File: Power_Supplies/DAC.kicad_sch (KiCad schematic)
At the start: 49 parts, among them J1 Line Out (Left), J2 Headphone Out, J21 Line Out (Right), U10 OPA2134, U11 TPA6110A2DGN, U34 NE5532AD, U35 NE5532AD, U9 PCM1780

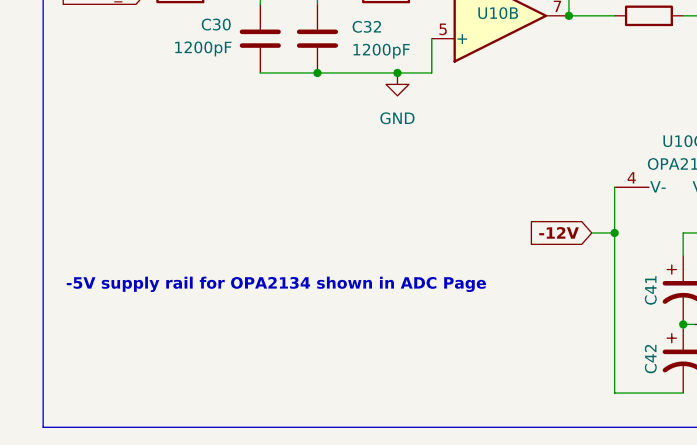
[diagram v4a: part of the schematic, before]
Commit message: Add files via upload
fixed voltage issues
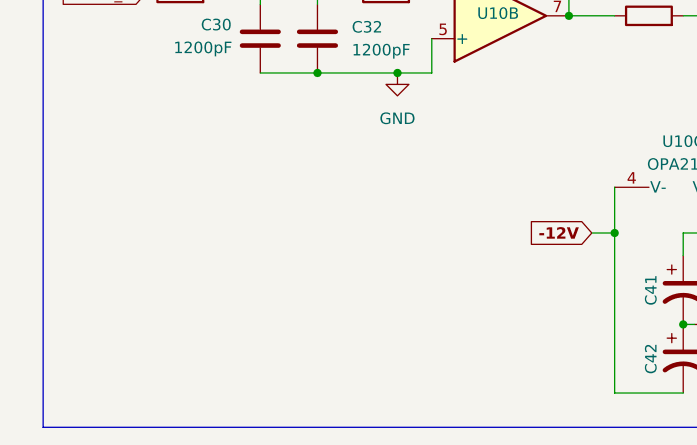
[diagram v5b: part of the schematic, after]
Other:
- note removed: "-5V supply rail for OPA2134 shown in ADC Page"
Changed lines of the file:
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@@
 		)
 	)
-	(text "-5V supply rail for OPA2134 shown in ADC Page\n"
-		(exclude_from_sim no)
-		(at 41.148 179.832 0)
-		(effects
-			(font
-				(size 1.27 1.27)
-				(bold yes)
-			)
-		)
-	)
 	(text "Headphone Amplifier \nUsing EVM Schematic as Ref.\n"
 		(exclude_from_sim no)
@@
 		(exclude_from_sim no)
 		(in_bom yes)
-		(on_board no)
+		(on_board yes)
 		(dnp no)
 		(fields_autoplaced yes)
@@
 		(exclude_from_sim no)
 		(in_bom yes)
-		(on_board no)
+		(on_board yes)
 		(dnp no)
 		(fields_autoplaced yes)
@@
 		(exclude_from_sim no)
 		(in_bom yes)
-		(on_board no)
+		(on_board yes)
 		(dnp no)
 		(fields_autoplaced yes)
@@
 		(exclude_from_sim no)
 		(in_bom yes)
-		(on_board no)
+		(on_board yes)
 		(dnp no)
 		(property "Reference" "C42"
@@
 		(exclude_from_sim no)
 		(in_bom yes)
-		(on_board no)
+		(on_board yes)
 		(dnp no)
 		(property "Reference" "C43"
@@
 		(exclude_from_sim no)
 		(in_bom yes)
-		(on_board no)
+		(on_board yes)
 		(dnp no)
 		(fields_autoplaced yes)
@@
 		(exclude_from_sim no)
 		(in_bom yes)
-		(on_board no)
+		(on_board yes)
 		(dnp no)
 		(property "Reference" "U34"
@@
 		(exclude_from_sim no)
 		(in_bom yes)
-		(on_board no)
+		(on_board yes)
 		(dnp no)
 		(fields_autoplaced yes)
@@
 		(exclude_from_sim no)
 		(in_bom yes)
-		(on_board no)
+		(on_board yes)
 		(dnp no)
 		(fields_autoplaced yes)
@@
 		(exclude_from_sim no)
 		(in_bom yes)
-		(on_board no)
+		(on_board yes)
 		(dnp no)
 		(property "Reference" "C41"
@@
 		(exclude_from_sim no)
 		(in_bom yes)
-		(on_board no)
+		(on_board yes)
 		(dnp no)
 		(property "Reference" "R24"
@@
 		(exclude_from_sim no)
 		(in_bom yes)
-		(on_board no)
+		(on_board yes)
 		(dnp no)
 		(property "Reference" "C33"
@@
 		(exclude_from_sim no)
 		(in_bom yes)
-		(on_board no)
+		(on_board yes)
 		(dnp no)
 		(fields_autoplaced yes)
@@
 		(exclude_from_sim no)
 		(in_bom yes)
-		(on_board no)
+		(on_board yes)
 		(dnp no)
 		(fields_autoplaced yes)
@@
 		(exclude_from_sim no)
 		(in_bom yes)
-		(on_board no)
+		(on_board yes)
 		(dnp no)
 		(property "Reference" "C29"
@@
 		(exclude_from_sim no)
 		(in_bom yes)
-		(on_board no)
+		(on_board yes)
 		(dnp no)
 		(property "Reference" "#PWR036"
@@
 		(exclude_from_sim no)
 		(in_bom yes)
-		(on_board no)
+		(on_board yes)
 		(dnp no)
 		(fields_autoplaced yes)
@@
 		(exclude_from_sim no)
 		(in_bom yes)
-		(on_board no)
+		(on_board yes)
 		(dnp no)
 		(fields_autoplaced yes)
@@
 		(exclude_from_sim no)
 		(in_bom yes)
-		(on_board no)
+		(on_board yes)
 		(dnp no)
 		(fields_autoplaced yes)
@@
 		(exclude_from_sim no)
 		(in_bom yes)
-		(on_board no)
+		(on_board yes)
 		(dnp no)
 		(fields_autoplaced yes)
@@
 		(exclude_from_sim no)
 		(in_bom yes)
-		(on_board no)
+		(on_board yes)
 		(dnp no)
 		(fields_autoplaced yes)
@@
 		(exclude_from_sim no)
 		(in_bom yes)
-		(on_board no)
+		(on_board yes)
 		(dnp no)
 		(property "Reference" "U10"
@@
 		(exclude_from_sim no)
 		(in_bom yes)
-		(on_board no)
+		(on_board yes)
 		(dnp no)
 		(fields_autoplaced yes)
@@
 		(exclude_from_sim no)
 		(in_bom yes)
-		(on_board no)
+		(on_board yes)
 		(dnp no)
 		(property "Reference" "C35"
@@
 		(exclude_from_sim no)
 		(in_bom yes)
-		(on_board no)
+		(on_board yes)
 		(dnp no)
 		(property "Reference" "U11"
@@
 		(exclude_from_sim no)
 		(in_bom yes)
-		(on_board no)
+		(on_board yes)
 		(dnp no)
 		(property "Reference" "R26"
@@
 		(exclude_from_sim no)
 		(in_bom yes)
-		(on_board no)
+		(on_board yes)
 		(dnp no)
 		(fields_autoplaced yes)
@@
 		(exclude_from_sim no)
 		(in_bom yes)
-		(on_board no)
+		(on_board yes)
 		(dnp no)
 		(fields_autoplaced yes)
@@
 		(exclude_from_sim no)
 		(in_bom yes)
-		(on_board no)
+		(on_board yes)
 		(dnp no)
 		(property "Reference" "C34"
@@
 		(exclude_from_sim no)
 		(in_bom yes)
-		(on_board no)
+		(on_board yes)
 		(dnp no)
 		(fields_autoplaced yes)
@@
 		(exclude_from_sim no)
 		(in_bom yes)
-		(on_board no)
+		(on_board yes)
 		(dnp no)
 		(property "Reference" "R30"
@@
 		(exclude_from_sim no)
 		(in_bom yes)
-		(on_board no)
+		(on_board yes)
 		(dnp no)
 		(fields_autoplaced yes)
@@
 		(exclude_from_sim no)
 		(in_bom yes)
-		(on_board no)
+		(on_board yes)
 		(dnp no)
 		(property "Reference" "R32"
@@
 		(exclude_from_sim no)
 		(in_bom yes)
-		(on_board no)
+		(on_board yes)
 		(dnp no)
 		(property "Reference" "U10"
@@
 		(exclude_from_sim no)
 		(in_bom yes)
-		(on_board no)
+		(on_board yes)
 		(dnp no)
 		(fields_autoplaced yes)
@@
 		(exclude_from_sim no)
 		(in_bom yes)
-		(on_board no)
+		(on_board yes)
 		(dnp no)
 		(fields_autoplaced yes)
@@
 		(exclude_from_sim no)
 		(in_bom yes)
-		(on_board no)
+		(on_board yes)
 		(dnp no)
 		(fields_autoplaced yes)
@@
 		(exclude_from_sim no)
 		(in_bom yes)
-		(on_board no)
+		(on_board yes)
 		(dnp no)
 		(property "Reference" "#PWR044"
@@
 		(exclude_from_sim no)
 		(in_bom yes)
-		(on_board no)
+		(on_board yes)
 		(dnp no)
 		(property "Reference" "U35"
@@
 		(exclude_from_sim no)
 		(in_bom yes)
-		(on_board no)
+		(on_board yes)
 		(dnp no)
 		(property "Reference" "R20"
@@
 		(exclude_from_sim no)
 		(in_bom yes)
-		(on_board no)
+		(on_board yes)
 		(dnp no)
 		(property "Reference" "C30"
@@
 		(exclude_from_sim no)
 		(in_bom yes)
-		(on_board no)
+		(on_board yes)
 		(dnp no)
 		(property "Reference" "R21"
@@
 		(exclude_from_sim no)
 		(in_bom yes)
-		(on_board no)
+		(on_board yes)
 		(dnp no)
 		(fields_autoplaced yes)
@@
 		(exclude_from_sim no)
 		(in_bom yes)
-		(on_board no)
+		(on_board yes)
 		(dnp no)
 		(property "Reference" "R22"
@@
 		(exclude_from_sim no)
 		(in_bom yes)
-		(on_board no)
+		(on_board yes)
 		(dnp no)
 		(fields_autoplaced yes)
@@
 		(exclude_from_sim no)
 		(in_bom yes)
-		(on_board no)
+		(on_board yes)
 		(dnp no)
 		(fields_autoplaced yes)
@@
 		(exclude_from_sim no)
 		(in_bom yes)
-		(on_board no)
+		(on_board yes)
 		(dnp no)
 		(fields_autoplaced yes)
@@
 		(exclude_from_sim no)
 		(in_bom yes)
-		(on_board no)
+		(on_board yes)
 		(dnp no)
 		(fields_autoplaced yes)
@@
 		(exclude_from_sim no)
 		(in_bom yes)
-		(on_board no)
+		(on_board yes)
 		(dnp no)
 		(fields_autoplaced yes)
@@
 		(exclude_from_sim no)
 		(in_bom yes)
-		(on_board no)
+		(on_board yes)
 		(dnp no)
 		(property "Reference" "R19"
@@
 		(exclude_from_sim no)
 		(in_bom yes)
-		(on_board no)
+		(on_board yes)
 		(dnp no)
 		(fields_autoplaced yes)
@@
 		(exclude_from_sim no)
 		(in_bom yes)
-		(on_board no)
+		(on_board yes)
 		(dnp no)
 		(property "Reference" "C40"
@@
 		(exclude_from_sim no)
 		(in_bom yes)
-		(on_board no)
+		(on_board yes)
 		(dnp no)
 		(property "Reference" "C47"
@@
 		(exclude_from_sim no)
 		(in_bom yes)
-		(on_board no)
+		(on_board yes)
 		(dnp no)
 		(fields_autoplaced yes)
@@
 		(exclude_from_sim no)
 		(in_bom yes)
-		(on_board no)
+		(on_board yes)
 		(dnp no)
 		(fields_autoplaced yes)
@@
 		(exclude_from_sim no)
 		(in_bom yes)
-		(on_board no)
+		(on_board yes)
 		(dnp no)
 		(property "Reference" "C39"
@@
 		(exclude_from_sim no)
 		(in_bom yes)
-		(on_board no)
+		(on_board yes)
 		(dnp no)
 		(property "Reference" "U10"
@@
 		(exclude_from_sim no)
 		(in_bom yes)
-		(on_board no)
+		(on_board yes)
 		(dnp no)
 		(fields_autoplaced yes)
@@
 		(exclude_from_sim no)
 		(in_bom yes)
-		(on_board no)
+		(on_board yes)
 		(dnp no)
 		(property "Reference" "R23"
@@
 		(exclude_from_sim no)
 		(in_bom yes)
-		(on_board no)
+		(on_board yes)
 		(dnp no)
 		(property "Reference" "C45"
@@
 		(exclude_from_sim no)
 		(in_bom yes)
-		(on_board no)
+		(on_board yes)
 		(dnp no)
 		(property "Reference" "R25"
@@
 		(exclude_from_sim no)
 		(in_bom yes)
-		(on_board no)
+		(on_board yes)
 		(dnp no)
 		(fields_autoplaced yes)
@@
 		(exclude_from_sim no)
 		(in_bom yes)
-		(on_board no)
+		(on_board yes)
 		(dnp no)
 		(fields_autoplaced yes)
@@
 		(exclude_from_sim no)
 		(in_bom yes)
-		(on_board no)
+		(on_board yes)
 		(dnp no)
 		(fields_autoplaced yes)
@@
 		(exclude_from_sim no)
 		(in_bom yes)
-		(on_board no)
+		(on_board yes)
 		(dnp no)
 		(property "Reference" "C36"
@@
 		(exclude_from_sim no)
 		(in_bom yes)
-		(on_board no)
+		(on_board yes)
 		(dnp no)
 		(fields_autoplaced yes)

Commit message: connected ADC/DACs, USB
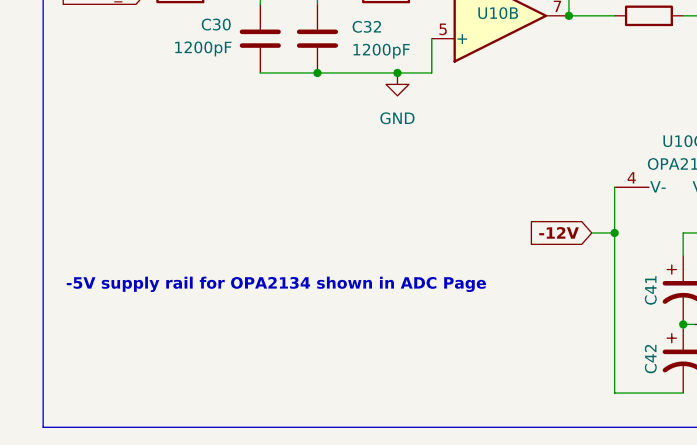
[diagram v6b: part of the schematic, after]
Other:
- note added: "-5V supply rail for OPA2134 shown in ADC Page"
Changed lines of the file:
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@@
 		)
 	)
+	(text "-5V supply rail for OPA2134 shown in ADC Page\n"
+		(exclude_from_sim no)
+		(at 41.148 179.832 0)
+		(effects
+			(font
+				(size 1.27 1.27)
+				(bold yes)
+			)
+		)
+	)
 	(text "Headphone Amplifier \nUsing EVM Schematic as Ref.\n"
 		(exclude_from_sim no)
@@
 		(exclude_from_sim no)
 		(in_bom yes)
-		(on_board yes)
+		(on_board no)
 		(dnp no)
 		(fields_autoplaced yes)
@@
 		(exclude_from_sim no)
 		(in_bom yes)
-		(on_board yes)
+		(on_board no)
 		(dnp no)
 		(fields_autoplaced yes)
@@
 		(exclude_from_sim no)
 		(in_bom yes)
-		(on_board yes)
+		(on_board no)
 		(dnp no)
 		(fields_autoplaced yes)
@@
 		(exclude_from_sim no)
 		(in_bom yes)
-		(on_board yes)
+		(on_board no)
 		(dnp no)
 		(property "Reference" "C42"
@@
 		(exclude_from_sim no)
 		(in_bom yes)
-		(on_board yes)
+		(on_board no)
 		(dnp no)
 		(property "Reference" "C43"
@@
 		(exclude_from_sim no)
 		(in_bom yes)
-		(on_board yes)
+		(on_board no)
 		(dnp no)
 		(fields_autoplaced yes)
@@
 		(exclude_from_sim no)
 		(in_bom yes)
-		(on_board yes)
+		(on_board no)
 		(dnp no)
 		(property "Reference" "U34"
@@
 		(exclude_from_sim no)
 		(in_bom yes)
-		(on_board yes)
+		(on_board no)
 		(dnp no)
 		(fields_autoplaced yes)
@@
 		(exclude_from_sim no)
 		(in_bom yes)
-		(on_board yes)
+		(on_board no)
 		(dnp no)
 		(fields_autoplaced yes)
@@
 		(exclude_from_sim no)
 		(in_bom yes)
-		(on_board yes)
+		(on_board no)
 		(dnp no)
 		(property "Reference" "C41"
@@
 		(exclude_from_sim no)
 		(in_bom yes)
-		(on_board yes)
+		(on_board no)
 		(dnp no)
 		(property "Reference" "R24"
@@
 		(exclude_from_sim no)
 		(in_bom yes)
-		(on_board yes)
+		(on_board no)
 		(dnp no)
 		(property "Reference" "C33"
@@
 		(exclude_from_sim no)
 		(in_bom yes)
-		(on_board yes)
+		(on_board no)
 		(dnp no)
 		(fields_autoplaced yes)
@@
 		(exclude_from_sim no)
 		(in_bom yes)
-		(on_board yes)
+		(on_board no)
 		(dnp no)
 		(fields_autoplaced yes)
@@
 		(exclude_from_sim no)
 		(in_bom yes)
-		(on_board yes)
+		(on_board no)
 		(dnp no)
 		(property "Reference" "C29"
@@
 		(exclude_from_sim no)
 		(in_bom yes)
-		(on_board yes)
+		(on_board no)
 		(dnp no)
 		(property "Reference" "#PWR036"
@@
 		(exclude_from_sim no)
 		(in_bom yes)
-		(on_board yes)
+		(on_board no)
 		(dnp no)
 		(fields_autoplaced yes)
@@
 		(exclude_from_sim no)
 		(in_bom yes)
-		(on_board yes)
+		(on_board no)
 		(dnp no)
 		(fields_autoplaced yes)
@@
 		(exclude_from_sim no)
 		(in_bom yes)
-		(on_board yes)
+		(on_board no)
 		(dnp no)
 		(fields_autoplaced yes)
@@
 		(exclude_from_sim no)
 		(in_bom yes)
-		(on_board yes)
+		(on_board no)
 		(dnp no)
 		(fields_autoplaced yes)
@@
 		(exclude_from_sim no)
 		(in_bom yes)
-		(on_board yes)
+		(on_board no)
 		(dnp no)
 		(fields_autoplaced yes)
@@
 		(exclude_from_sim no)
 		(in_bom yes)
-		(on_board yes)
+		(on_board no)
 		(dnp no)
 		(property "Reference" "U10"
@@
 		(exclude_from_sim no)
 		(in_bom yes)
-		(on_board yes)
+		(on_board no)
 		(dnp no)
 		(fields_autoplaced yes)
@@
 		(exclude_from_sim no)
 		(in_bom yes)
-		(on_board yes)
+		(on_board no)
 		(dnp no)
 		(property "Reference" "C35"
@@
 		(exclude_from_sim no)
 		(in_bom yes)
-		(on_board yes)
+		(on_board no)
 		(dnp no)
 		(property "Reference" "U11"
@@
 		(exclude_from_sim no)
 		(in_bom yes)
-		(on_board yes)
+		(on_board no)
 		(dnp no)
 		(property "Reference" "R26"
@@
 		(exclude_from_sim no)
 		(in_bom yes)
-		(on_board yes)
+		(on_board no)
 		(dnp no)
 		(fields_autoplaced yes)
@@
 		(exclude_from_sim no)
 		(in_bom yes)
-		(on_board yes)
+		(on_board no)
 		(dnp no)
 		(fields_autoplaced yes)
@@
 		(exclude_from_sim no)
 		(in_bom yes)
-		(on_board yes)
+		(on_board no)
 		(dnp no)
 		(property "Reference" "C34"
@@
 		(exclude_from_sim no)
 		(in_bom yes)
-		(on_board yes)
+		(on_board no)
 		(dnp no)
 		(fields_autoplaced yes)
@@
 		(exclude_from_sim no)
 		(in_bom yes)
-		(on_board yes)
+		(on_board no)
 		(dnp no)
 		(property "Reference" "R30"
@@
 		(exclude_from_sim no)
 		(in_bom yes)
-		(on_board yes)
+		(on_board no)
 		(dnp no)
 		(fields_autoplaced yes)
@@
 		(exclude_from_sim no)
 		(in_bom yes)
-		(on_board yes)
+		(on_board no)
 		(dnp no)
 		(property "Reference" "R32"
@@
 		(exclude_from_sim no)
 		(in_bom yes)
-		(on_board yes)
+		(on_board no)
 		(dnp no)
 		(property "Reference" "U10"
@@
 		(exclude_from_sim no)
 		(in_bom yes)
-		(on_board yes)
+		(on_board no)
 		(dnp no)
 		(fields_autoplaced yes)
@@
 		(exclude_from_sim no)
 		(in_bom yes)
-		(on_board yes)
+		(on_board no)
 		(dnp no)
 		(fields_autoplaced yes)
@@
 		(exclude_from_sim no)
 		(in_bom yes)
-		(on_board yes)
+		(on_board no)
 		(dnp no)
 		(fields_autoplaced yes)
@@
 		(exclude_from_sim no)
 		(in_bom yes)
-		(on_board yes)
+		(on_board no)
 		(dnp no)
 		(property "Reference" "#PWR044"
@@
 		(exclude_from_sim no)
 		(in_bom yes)
-		(on_board yes)
+		(on_board no)
 		(dnp no)
 		(property "Reference" "U35"
@@
 		(exclude_from_sim no)
 		(in_bom yes)
-		(on_board yes)
+		(on_board no)
 		(dnp no)
 		(property "Reference" "R20"
@@
 		(exclude_from_sim no)
 		(in_bom yes)
-		(on_board yes)
+		(on_board no)
 		(dnp no)
 		(property "Reference" "C30"
@@
 		(exclude_from_sim no)
 		(in_bom yes)
-		(on_board yes)
+		(on_board no)
 		(dnp no)
 		(property "Reference" "R21"
@@
 		(exclude_from_sim no)
 		(in_bom yes)
-		(on_board yes)
+		(on_board no)
 		(dnp no)
 		(fields_autoplaced yes)
@@
 		(exclude_from_sim no)
 		(in_bom yes)
-		(on_board yes)
+		(on_board no)
 		(dnp no)
 		(property "Reference" "R22"
@@
 		(exclude_from_sim no)
 		(in_bom yes)
-		(on_board yes)
+		(on_board no)
 		(dnp no)
 		(fields_autoplaced yes)
@@
 		(exclude_from_sim no)
 		(in_bom yes)
-		(on_board yes)
+		(on_board no)
 		(dnp no)
 		(fields_autoplaced yes)
@@
 		(exclude_from_sim no)
 		(in_bom yes)
-		(on_board yes)
+		(on_board no)
 		(dnp no)
 		(fields_autoplaced yes)
@@
 		(exclude_from_sim no)
 		(in_bom yes)
-		(on_board yes)
+		(on_board no)
 		(dnp no)
 		(fields_autoplaced yes)
@@
 		(exclude_from_sim no)
 		(in_bom yes)
-		(on_board yes)
+		(on_board no)
 		(dnp no)
 		(fields_autoplaced yes)
@@
 		(exclude_from_sim no)
 		(in_bom yes)
-		(on_board yes)
+		(on_board no)
 		(dnp no)
 		(property "Reference" "R19"
@@
 		(exclude_from_sim no)
 		(in_bom yes)
-		(on_board yes)
+		(on_board no)
 		(dnp no)
 		(fields_autoplaced yes)
@@
 		(exclude_from_sim no)
 		(in_bom yes)
-		(on_board yes)
+		(on_board no)
 		(dnp no)
 		(property "Reference" "C40"
@@
 		(exclude_from_sim no)
 		(in_bom yes)
-		(on_board yes)
+		(on_board no)
 		(dnp no)
 		(property "Reference" "C47"
@@
 		(exclude_from_sim no)
 		(in_bom yes)
-		(on_board yes)
+		(on_board no)
 		(dnp no)
 		(fields_autoplaced yes)
@@
 		(exclude_from_sim no)
 		(in_bom yes)
-		(on_board yes)
+		(on_board no)
 		(dnp no)
 		(fields_autoplaced yes)
@@
 		(exclude_from_sim no)
 		(in_bom yes)
-		(on_board yes)
+		(on_board no)
 		(dnp no)
 		(property "Reference" "C39"
@@
 		(exclude_from_sim no)
 		(in_bom yes)
-		(on_board yes)
+		(on_board no)
 		(dnp no)
 		(property "Reference" "U10"
@@
 		(exclude_from_sim no)
 		(in_bom yes)
-		(on_board yes)
+		(on_board no)
 		(dnp no)
 		(fields_autoplaced yes)
@@
 		(exclude_from_sim no)
 		(in_bom yes)
-		(on_board yes)
+		(on_board no)
 		(dnp no)
 		(property "Reference" "R23"
@@
 		(exclude_from_sim no)
 		(in_bom yes)
-		(on_board yes)
+		(on_board no)
 		(dnp no)
 		(property "Reference" "C45"
@@
 		(exclude_from_sim no)
 		(in_bom yes)
-		(on_board yes)
+		(on_board no)
 		(dnp no)
 		(property "Reference" "R25"
@@
 		(exclude_from_sim no)
 		(in_bom yes)
-		(on_board yes)
+		(on_board no)
 		(dnp no)
 		(fields_autoplaced yes)
@@
 		(exclude_from_sim no)
 		(in_bom yes)
-		(on_board yes)
+		(on_board no)
 		(dnp no)
 		(fields_autoplaced yes)
@@
 		(exclude_from_sim no)
 		(in_bom yes)
-		(on_board yes)
+		(on_board no)
 		(dnp no)
 		(fields_autoplaced yes)
@@
 		(exclude_from_sim no)
 		(in_bom yes)
-		(on_board yes)
+		(on_board no)
 		(dnp no)
 		(property "Reference" "C36"
@@
 		(exclude_from_sim no)
 		(in_bom yes)
-		(on_board yes)
+		(on_board no)
 		(dnp no)
 		(fields_autoplaced yes)

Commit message: Add files via upload
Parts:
- added J33: PINHD_1x3_Female, Connector_PinSocket_2.54mm:PinSocket_1x03_P2.54mm_Vertical, symbol PCM_SL_Pin_Headers:PINHD_1x3_Female
- added J36: PINHD_1x2_Female, Connector_PinSocket_2.54mm:PinSocket_1x02_P2.54mm_Vertical, symbol PCM_SL_Pin_Headers:PINHD_1x2_Female
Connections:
- net MODE_CONTROL_CLOCK: no longer names the net of U9.3 (MC)
- net MODE_CONTROL_CLOCK: now also J33.2
- net MODE_CONTROL_DATA: no longer names the net of U9.4 (MD)
- net MODE_CONTROL_DATA: now also J33.3
- net MODE_CONTROL_SELECT: no longer names the net of U9.2 (~{MS})
- net MODE_CONTROL_SELECT: now also J33.1
- net ZERO_L: no longer names the net of U9.1 (ZEROL)
- net ZERO_L: now also J36.1
- net ZERO_R: no longer names the net of U9.16 (ZEROR)
- net ZERO_R: now also J36.2
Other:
- note removed: "-5V supply rail for OPA2134 shown in ADC Page"
